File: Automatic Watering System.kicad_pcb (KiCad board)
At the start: 2 copper layers, 6 parts, among them J1 691137710002, J2 691137710002, U1 DFR0654

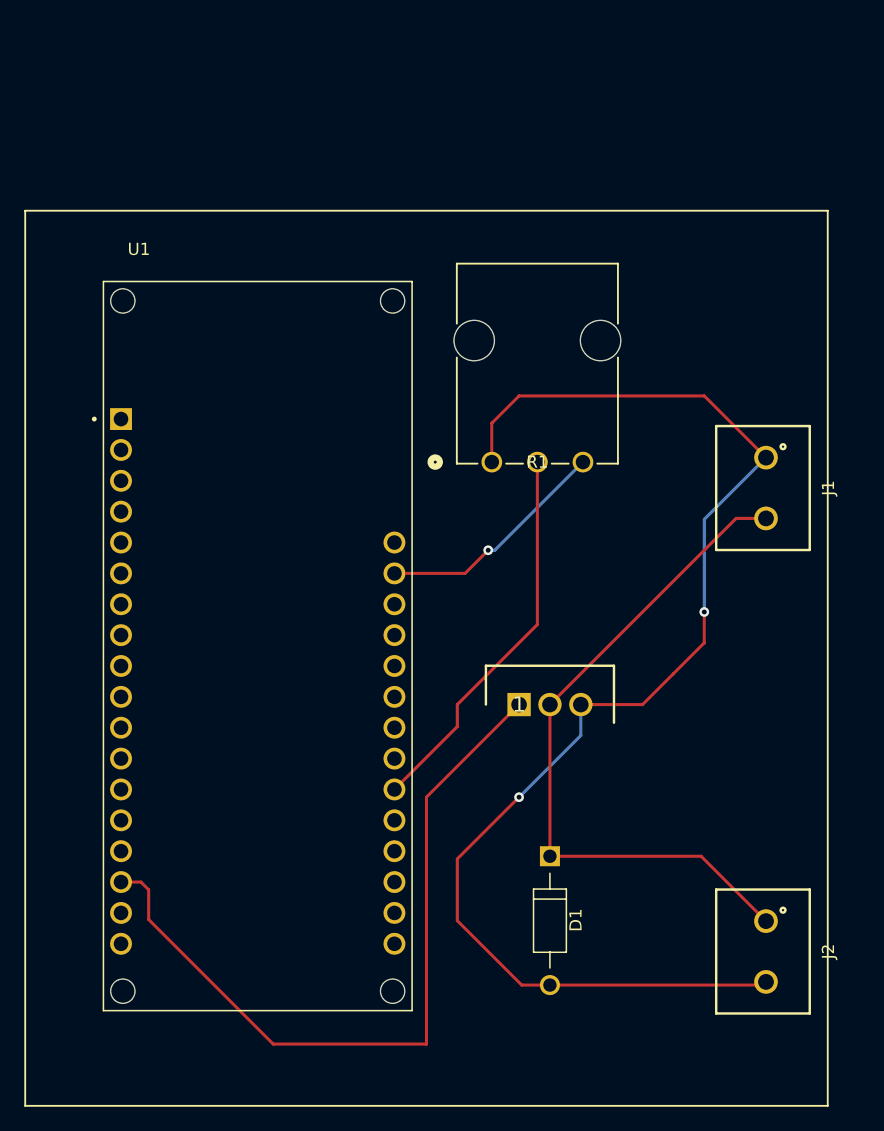
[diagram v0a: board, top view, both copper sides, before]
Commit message: Fixing some issues with schematics and changing potentiometer
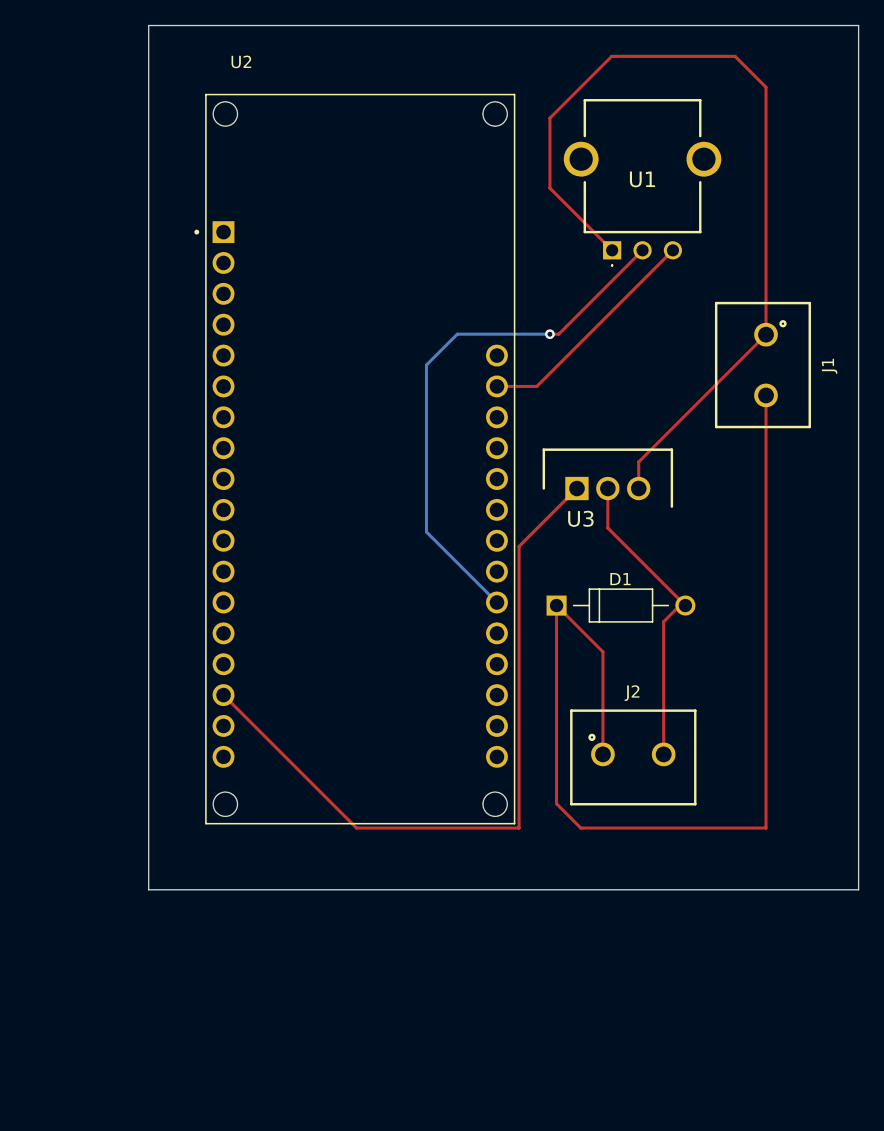
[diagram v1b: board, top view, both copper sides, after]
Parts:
- removed 1: IRLZ44NPBF, Imported:TO254P469X1042X1967-3P
- removed R1: P120PK-Y25BR10K, Imported:POT_P120PK-x25_TTE
- added U2: DFR0654, Imported:MODULE_DFR0654, F.Cu at (96.2, 73.8)
- added U3: IRLZ44NPBF, Imported:TO254P469X1042X1967-3P, F.Cu at (114.0, 76.2)
- U1: value DFR0654 -> PTN091-V10115K1B; footprint Imported:MODULE_DFR0654 -> Imported:PTN091V10115K1B
- moved U1 43.7 mm to (116.9, 56.6)
- moved D1 26.6 mm to (117.6, 85.8), turned to 0 degrees
- moved J2 19.6 mm to (118.6, 98.1), turned to 0 degrees
- moved J1 10.1 mm to (129.5, 66.0)
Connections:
- D1 pad A: Net-(1-Pad3) -> Net-(D1-PadA)
- J1 pad 1: Net-(1-Pad3) -> Net-(J1-Pad1)
- J2 pad 2: Net-(1-Pad3) -> Net-(D1-PadA)
- U1 pad 1: unconnected-(U1-Pad1) -> Net-(J1-Pad1)
- U1 pad 2: Net-(R1-Pad3) -> Net-(U1-Pad2)
- U1 pad 3: unconnected-(U1-Pad3) -> Net-(U1-Pad3)
- U1 pad 4: unconnected-(U1-Pad30) -> unconnected-(U1-Pad4)
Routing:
- net Net-(1-Pad3): track 108.1 -> 0.00 mm, vias 2 -> 0
- net Net-(J1-Pad1): track 0.00 -> 71.3 mm
- net Net-(1-Pad1): track 63.2 -> 0.00 mm
- net Net-(U2-Pad16): track 0.00 -> 58.8 mm
- net Net-(U1-Pad2): track 0.00 -> 43.6 mm, vias 0 -> 1
- net Net-(R1-Pad2): track 31.8 -> 0.00 mm
- net Net-(D1-PadC): track 56.6 -> 83.8 mm
- net Net-(D1-PadA): track 0.00 -> 25.5 mm
- net Net-(R1-Pad3): track 19.3 -> 0.00 mm, vias 1 -> 0
- net Net-(U1-Pad3): track 0.00 -> 19.1 mm
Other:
- board outline added: 58.4 x 71.1 mm

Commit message: minor changes
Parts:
- moved J1 15.3 mm to (129.5, 81.3), turned to 90 degrees
- moved D1 8.99 mm to (118.1, 94.8), turned to 180 degrees
- moved J2 4.50 mm to (118.6, 102.6), turned to 180 degrees
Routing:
- net Net-(D1-PadC): track 83.8 -> 34.5 mm
- net Net-(J1-Pad1): track 71.3 -> 84.9 mm
- net Net-(D1-PadA): track 25.5 -> 29.3 mm
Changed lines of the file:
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@@
     (pad "32" thru_hole circle (at 11.25 -8.52) (size 1.8 1.8) (drill 1.2) (layers *.Cu *.Mask)
       (net 32 "unconnected-(U2-Pad32)") (pinfunction "VCC") (pintype "power_in+no_connect") (solder_mask_margin 0.102))
+    (model "${KIPRJMOD}/DFR0654--3DModel-STEP-56544.STEP"
+      (offset (xyz 0 0 0))
+      (scale (xyz 1 1 1))
+      (rotate (xyz -90 0 0))
+    )
   )
   (footprint "Imported:DIOAD1060W80L520D270" (layer "F.Cu")
-    (at 117.605 85.83)
+    (at 118.1425 94.8 180)
     (property "MANUFACTURER" "ON Semiconductor")
     (property "PARTREV" "G")
@@
     (fp_line (start 2.6 0) (end 2.6 -1.35) (layer "F.Fab") (width 0.127))
     (fp_line (start -1.775 1.35) (end -1.775 -1.35) (layer "F.Fab") (width 0.127))
-    (pad "A" thru_hole circle (at 5.3 0) (size 1.65 1.65) (drill 1.1) (layers *.Cu *.Mask)
+    (pad "A" thru_hole circle (at 5.3 0 180) (size 1.65 1.65) (drill 1.1) (layers *.Cu *.Mask)
       (net 1 "Net-(D1-PadA)") (pintype "passive") (solder_mask_margin 0.102))
-    (pad "C" thru_hole rect (at -5.3 0) (size 1.65 1.65) (drill 1.1) (layers *.Cu *.Mask)
+    (pad "C" thru_hole rect (at -5.3 0 180) (size 1.65 1.65) (drill 1.1) (layers *.Cu *.Mask)
       (net 2 "Net-(D1-PadC)") (pintype "passive") (solder_mask_margin 0.102))
   )
@@
       (rotate (xyz 0 0 0))
     )
+    (model "${KIPRJMOD}/LIB_IRLZ44NPBF/IRLZ44NPBF/3D/IRLZ44NPBF.stp"
+      (offset (xyz 0 0 0))
+      (scale (xyz 1 1 1))
+      (rotate (xyz 0 0 0))
+    )
   )
   (footprint "Imported:691137710002" (layer "F.Cu")
-    (at 118.62 98.08)
+    (at 118.62 102.58 180)
     (property "Sheetfile" "Automatic Watering System.kicad_sch")
     (property "Sheetname" "")
@@
     (fp_line (start -5 4) (end -5 -3.5) (layer "F.Fab") (width 0.1))
     (fp_line (start 5 -3.5) (end 5 4) (layer "F.Fab") (width 0.1))
-    (pad "1" thru_hole circle (at -2.5 0) (size 1.95 1.95) (drill 1.3) (layers *.Cu *.Mask)
+    (pad "1" thru_hole circle (at -2.5 0 180) (size 1.95 1.95) (drill 1.3) (layers *.Cu *.Mask)
       (net 2 "Net-(D1-PadC)") (pintype "passive") (solder_mask_margin 0.102))
-    (pad "2" thru_hole circle (at 2.5 0) (size 1.95 1.95) (drill 1.3) (layers *.Cu *.Mask)
+    (pad "2" thru_hole circle (at 2.5 0 180) (size 1.95 1.95) (drill 1.3) (layers *.Cu *.Mask)
       (net 1 "Net-(D1-PadA)") (pintype "passive") (solder_mask_margin 0.102))
+    (model "${KIPRJMOD}/691137710002/691137710002.step"
+      (offset (xyz -5 -4 0))
+      (scale (xyz 1 1 1))
+      (rotate (xyz 90 180 -90))
+    )
   )
   (footprint "Imported:691137710002" (layer "F.Cu")
-    (at 129.54 66.04 -90)
+    (at 129.54 81.32 90)
     (property "Sheetfile" "Automatic Watering System.kicad_sch")
     (property "Sheetname" "")
@@
     (fp_line (start -5 -3.5) (end 5 -3.5) (layer "F.Fab") (width 0.1))
     (fp_line (start 5 4) (end -5 4) (layer "F.Fab") (width 0.1))
-    (pad "1" thru_hole circle (at -2.5 0 270) (size 1.95 1.95) (drill 1.3) (layers *.Cu *.Mask)
+    (pad "1" thru_hole circle (at -2.5 0 90) (size 1.95 1.95) (drill 1.3) (layers *.Cu *.Mask)
       (net 33 "Net-(J1-Pad1)") (pintype "passive") (solder_mask_margin 0.102))
-    (pad "2" thru_hole circle (at 2.5 0 270) (size 1.95 1.95) (drill 1.3) (layers *.Cu *.Mask)
+    (pad "2" thru_hole circle (at 2.5 0 90) (size 1.95 1.95) (drill 1.3) (layers *.Cu *.Mask)
       (net 2 "Net-(D1-PadC)") (pintype "passive") (solder_mask_margin 0.102))
+    (model "${KIPRJMOD}/691137710002/691137710002.step"
+      (offset (xyz -5 -4 0))
+      (scale (xyz 1 1 1))
+      (rotate (xyz 90 -180 -90))
+    )
   )
   (footprint "Imported:PTN091V10115K1B" (layer "F.Cu")
@@
       (rotate (xyz 90 0 0))
     )
+    (model "${KIPRJMOD}/LIB_PTN091-V10115K1B/PTN091-V10115K1B/3D/PTN091-V10115K1B.stp"
+      (offset (xyz 2.5 7.5 10))
+      (scale (xyz 1 1 1))
+      (rotate (xyz 90 0 0))
+    )
   )
   (gr_rect (start 78.74 38.1) (end 137.16 109.22) (layer "Edge.Cuts") (width 0.1) (fill none))
-  (segment (start 116.525 79.45) (end 116.525 76.2) (width 0.25) (layer "F.Cu") (net 1))
-  (segment (start 122.45 85.83) (end 122.905 85.83) (width 0.25) (layer "F.Cu") (net 1))
-  (segment (start 122.905 85.83) (end 116.525 79.45) (width 0.25) (layer "F.Cu") (net 1))
-  (segment (start 121.12 98.08) (end 121.12 87.16) (width 0.25) (layer "F.Cu") (net 1))
-  (segment (start 121.12 87.16) (end 122.45 85.83) (width 0.25) (layer "F.Cu") (net 1))
-  (segment (start 116.12 89.645) (end 112.305 85.83) (width 0.25) (layer "F.Cu") (net 2))
-  (segment (start 112.305 85.83) (end 112.305 102.145) (width 0.25) (layer "F.Cu") (net 2))
-  (segment (start 114.3 104.14) (end 129.54 104.14) (width 0.25) (layer "F.Cu") (net 2))
-  (segment (start 116.12 98.08) (end 116.12 89.645) (width 0.25) (layer "F.Cu") (net 2))
-  (segment (start 112.305 102.145) (end 114.3 104.14) (width 0.25) (layer "F.Cu") (net 2))
-  (segment (start 129.54 104.14) (end 129.54 68.54) (width 0.25) (layer "F.Cu") (net 2))
+  (segment (start 116.525 76.515) (end 116.525 76.2) (width 0.25) (layer "F.Cu") (net 1))
+  (segment (start 114.3 78.74) (end 116.525 76.515) (width 0.25) (layer "F.Cu") (net 1))
+  (segment (start 112.8425 99.3025) (end 112.8425 94.8) (width 0.25) (layer "F.Cu") (net 1))
+  (segment (start 116.12 102.58) (end 112.8425 99.3025) (width 0.25) (layer "F.Cu") (net 1))
+  (segment (start 112.8425 94.8) (end 112.8425 82.7375) (width 0.25) (layer "F.Cu") (net 1))
+  (segment (start 114.3 81.28) (end 114.3 78.74) (width 0.25) (layer "F.Cu") (net 1))
+  (segment (start 112.8425 82.7375) (end 114.3 81.28) (width 0.25) (layer "F.Cu") (net 1))
+  (segment (start 123.4425 94.8) (end 128.72 94.8) (width 0.25) (layer "F.Cu") (net 2))
+  (segment (start 134.62 88.9) (end 134.62 83.9) (width 0.25) (layer "F.Cu") (net 2))
+  (segment (start 121.12 97.1225) (end 123.4425 94.8) (width 0.25) (layer "F.Cu") (net 2))
+  (segment (start 134.62 83.9) (end 129.54 78.82) (width 0.25) (layer "F.Cu") (net 2))
+  (segment (start 121.12 102.58) (end 121.12 97.1225) (width 0.25) (layer "F.Cu") (net 2))
+  (segment (start 128.72 94.8) (end 134.62 88.9) (width 0.25) (layer "F.Cu") (net 2))
   (segment (start 112.48 63.5) (end 111.76 63.5) (width 0.25) (layer "F.Cu") (net 3))
   (segment (start 119.38 56.6) (end 112.48 63.5) (width 0.25) (layer "F.Cu") (net 3))
@@
   (segment (start 116.84 40.64) (end 111.76 45.72) (width 0.25) (layer "F.Cu") (net 33))
   (segment (start 129.54 43.18) (end 127 40.64) (width 0.25) (layer "F.Cu") (net 33))
+  (segment (start 126.685 83.82) (end 119.065 76.2) (width 0.25) (layer "F.Cu") (net 33))
   (segment (start 111.76 51.48) (end 116.88 56.6) (width 0.25) (layer "F.Cu") (net 33))
   (segment (start 119.065 76.2) (end 119.065 74.015) (width 0.25) (layer "F.Cu") (net 33))
   (segment (start 129.54 63.54) (end 129.54 43.18) (width 0.25) (layer "F.Cu") (net 33))
   (segment (start 111.76 45.72) (end 111.76 51.48) (width 0.25) (layer "F.Cu") (net 33))
+  (segment (start 129.54 83.82) (end 126.685 83.82) (width 0.25) (layer "F.Cu") (net 33))
 )

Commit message: fixing some issues with  the pcb
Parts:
- moved J2 2.03 mm to (116.8, 101.6), turned to 0 degrees
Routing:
- net Net-(D1-PadC): track 34.5 -> 48.1 mm
- net Net-(D1-PadA): track 29.3 -> 30.3 mm
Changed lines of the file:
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@@
       (layerselection 0x00010fc_ffffffff)
       (disableapertmacros false)
-      (usegerberextensions false)
+      (usegerberextensions true)
       (usegerberattributes true)
       (usegerberadvancedattributes true)
@@
       (plotinvisibletext false)
       (sketchpadsonfab false)
-      (subtractmaskfromsilk false)
+      (subtractmaskfromsilk true)
       (outputformat 1)
       (mirror false)
@@
   )
   (footprint "Imported:691137710002" (layer "F.Cu")
-    (at 118.62 102.58 180)
+    (at 116.84 101.6)
     (property "Sheetfile" "Automatic Watering System.kicad_sch")
     (property "Sheetname" "")
@@
     (fp_line (start -5 4) (end -5 -3.5) (layer "F.Fab") (width 0.1))
     (fp_line (start 5 -3.5) (end 5 4) (layer "F.Fab") (width 0.1))
-    (pad "1" thru_hole circle (at -2.5 0 180) (size 1.95 1.95) (drill 1.3) (layers *.Cu *.Mask)
+    (pad "1" thru_hole circle (at -2.5 0) (size 1.95 1.95) (drill 1.3) (layers *.Cu *.Mask)
       (net 2 "Net-(D1-PadC)") (pintype "passive") (solder_mask_margin 0.102))
-    (pad "2" thru_hole circle (at 2.5 0 180) (size 1.95 1.95) (drill 1.3) (layers *.Cu *.Mask)
+    (pad "2" thru_hole circle (at 2.5 0) (size 1.95 1.95) (drill 1.3) (layers *.Cu *.Mask)
       (net 1 "Net-(D1-PadA)") (pintype "passive") (solder_mask_margin 0.102))
     (model "${KIPRJMOD}/691137710002/691137710002.step"
@@
   (segment (start 116.525 76.515) (end 116.525 76.2) (width 0.25) (layer "F.Cu") (net 1))
   (segment (start 114.3 78.74) (end 116.525 76.515) (width 0.25) (layer "F.Cu") (net 1))
-  (segment (start 112.8425 99.3025) (end 112.8425 94.8) (width 0.25) (layer "F.Cu") (net 1))
-  (segment (start 116.12 102.58) (end 112.8425 99.3025) (width 0.25) (layer "F.Cu") (net 1))
+  (segment (start 112.8425 94.8) (end 119.34 101.2975) (width 0.25) (layer "F.Cu") (net 1))
+  (segment (start 119.34 101.2975) (end 119.34 101.6) (width 0.25) (layer "F.Cu") (net 1))
   (segment (start 112.8425 94.8) (end 112.8425 82.7375) (width 0.25) (layer "F.Cu") (net 1))
+  (segment (start 112.8425 95.4375) (end 112.8425 94.8) (width 0.25) (layer "F.Cu") (net 1))
   (segment (start 114.3 81.28) (end 114.3 78.74) (width 0.25) (layer "F.Cu") (net 1))
   (segment (start 112.8425 82.7375) (end 114.3 81.28) (width 0.25) (layer "F.Cu") (net 1))
   (segment (start 123.4425 94.8) (end 128.72 94.8) (width 0.25) (layer "F.Cu") (net 2))
+  (segment (start 114.34 104.1) (end 114.34 101.6) (width 0.25) (layer "F.Cu") (net 2))
+  (segment (start 119.38 106.68) (end 116.84 106.68) (width 0.25) (layer "F.Cu") (net 2))
+  (segment (start 123.4425 94.8) (end 123.4425 102.6175) (width 0.25) (layer "F.Cu") (net 2))
   (segment (start 134.62 88.9) (end 134.62 83.9) (width 0.25) (layer "F.Cu") (net 2))
-  (segment (start 121.12 97.1225) (end 123.4425 94.8) (width 0.25) (layer "F.Cu") (net 2))
+  (segment (start 114.3 104.14) (end 114.34 104.1) (width 0.25) (layer "F.Cu") (net 2))
   (segment (start 134.62 83.9) (end 129.54 78.82) (width 0.25) (layer "F.Cu") (net 2))
-  (segment (start 121.12 102.58) (end 121.12 97.1225) (width 0.25) (layer "F.Cu") (net 2))
+  (segment (start 123.4425 102.6175) (end 119.38 106.68) (width 0.25) (layer "F.Cu") (net 2))
+  (segment (start 116.84 106.68) (end 114.3 104.14) (width 0.25) (layer "F.Cu") (net 2))
   (segment (start 128.72 94.8) (end 134.62 88.9) (width 0.25) (layer "F.Cu") (net 2))
   (segment (start 112.48 63.5) (end 111.76 63.5) (width 0.25) (layer "F.Cu") (net 3))

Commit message: Add files via upload
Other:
- outline, holes or cut-outs redrawn
- board text added: "Diode"
- board text added: "ESP32"
- board text added: "MOSFET"
- board text added: "Potentiometer"
- board text added: "Power Source"
- board text added: "Water Pump"
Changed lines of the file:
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@@
     )
   )
-  (gr_rect (start 78.74 38.1) (end 137.16 109.22) (layer "Edge.Cuts") (width 0.1) (fill none))
+  (gr_line (start 78.74 40.64) (end 78.74 106.68) (layer "Edge.Cuts") (width 0.1))
+  (gr_arc (start 134.62 38.1) (mid 136.416051 38.843949) (end 137.16 40.64) (layer "Edge.Cuts") (width 0.2))
+  (gr_arc (start 78.74 40.64) (mid 79.483949 38.843949) (end 81.28 38.1) (layer "Edge.Cuts") (width 0.1))
+  (gr_line (start 134.62 109.22) (end 81.28 109.22) (layer "Edge.Cuts") (width 0.1))
+  (gr_arc (start 137.16 106.68) (mid 136.416051 108.476051) (end 134.62 109.22) (layer "Edge.Cuts") (width 0.1))
+  (gr_line (start 137.16 106.68) (end 137.16 40.64) (layer "Edge.Cuts") (width 0.1))
+  (gr_arc (start 81.28 109.22) (mid 79.483949 108.476051) (end 78.74 106.68) (layer "Edge.Cuts") (width 0.1))
+  (gr_line (start 134.62 38.1) (end 81.28 38.1) (layer "Edge.Cuts") (width 0.1))
+  (gr_text "Power Source\n" (at 132.08 68.58 90) (layer "F.SilkS")
+    (effects (font (size 1 1) (thickness 0.15)))
+  )
+  (gr_text "Potentiometer\n" (at 132.08 50.8 90) (layer "F.SilkS")
+    (effects (font (size 1 1) (thickness 0.15)))
+  )
+  (gr_text "Water Pump" (at 129.54 101.6) (layer "F.SilkS")
+    (effects (font (size 1 1) (thickness 0.15)))
+  )
+  (gr_text "MOSFET" (at 116.84 71.12) (layer "F.SilkS")
+    (effects (font (size 1 1) (thickness 0.15)))
+  )
+  (gr_text "ESP32\n" (at 96.52 73.66) (layer "F.SilkS")
+    (effects (font (size 1 1) (thickness 0.15)))
+  )
+  (gr_text "Diode" (at 119.38 91.44) (layer "Edge.Cuts")
+    (effects (font (size 1 1) (thickness 0.15)))
+  )
   (segment (start 116.525 76.515) (end 116.525 76.2) (width 0.25) (layer "F.Cu") (net 1))
   (segment (start 114.3 78.74) (end 116.525 76.515) (width 0.25) (layer "F.Cu") (net 1))
